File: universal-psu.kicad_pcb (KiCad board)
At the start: 2 copper layers, 64 parts, among them J1 Screw_Terminal_01x04, J2 Screw_Terminal_01x04, J3 Screw_Terminal_01x04

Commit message: layout changes
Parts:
- moved C15 139.9 mm to (264.7, 138.4)
- moved C18 139.9 mm to (258.2, 118.3)
- moved C19 139.9 mm to (258.2, 122.6)
- moved C20 139.9 mm to (258.2, 126.8)
- moved C22 139.9 mm to (264.7, 140.2)
- moved PS3 139.9 mm to (263.1, 133.2)
- moved R12 139.9 mm to (247.6, 120.0)
- moved R15 139.9 mm to (247.6, 127.5)
- moved 12V2 139.9 mm to (251.8, 131.0)
- moved 3v3 139.9 mm to (255.8, 139.1)
- moved 3v3_FB1 139.9 mm to (251.8, 139.1)
- moved 3v3_RT1 139.9 mm to (255.8, 131.0)
- moved C13 139.9 mm to (252.6, 118.3)
- moved C14 139.9 mm to (252.6, 122.6)
- moved C16 139.9 mm to (259.7, 140.3)
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- renumbered TP1 to 12V1, TP8 to 12V2, TP14 to 3v3, TP10 to 3v3_FB1, TP12 to 3v3_RT1, TP7 to 5V1, TP3 to 5V_FB1, TP5 to 5V_RT1, TP2 to GND1, TP4 to GND2, TP6 to GND3, TP9 to GND4, TP11 to GND5, TP13 to GND6
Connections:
- R8 pad 1: +5V -> +3V3
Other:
- copper layers 2 -> 4

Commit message: more  layout
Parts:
- moved C16 171.3 mm to (178.1, -10.3)
- moved C18 171.3 mm to (176.6, -32.2)
- moved C19 171.3 mm to (176.6, -28.0)
- moved C20 171.3 mm to (176.6, -23.8)
- moved GND4 171.3 mm to (170.2, -15.6)
- moved GND6 171.3 mm to (174.2, -15.6)
- moved R18 171.3 mm to (165.9, -15.6)
- moved 12V2 171.3 mm to (170.2, -19.6)
- moved 3v3 171.3 mm to (174.2, -11.5)
- moved 3v3_FB1 171.3 mm to (170.2, -11.5)
- moved 3v3_RT1 171.3 mm to (174.2, -19.6)
- moved C13 171.3 mm to (170.9, -32.2)
- moved C14 171.3 mm to (170.9, -28.0)
- moved C15 171.3 mm to (183.1, -12.2)
- moved C17 171.3 mm to (170.9, -23.8)
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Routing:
- net /DC_DC_Converter_5V/FB: track 0.00 -> 19.0 mm
- net /DC_DC_Converter_5V/Vosns: track 0.00 -> 12.7 mm
- net /DC_DC_Converter_5V/Vcc: track 0.00 -> 11.4 mm
- net /DC_DC_Converter_5V/COMP: track 0.00 -> 10.5 mm
- net /DC_DC_Converter_5V/RT: track 0.00 -> 10.0 mm
- net /DC_DC_Converter_5V/PG: track 0.00 -> 9.96 mm
- net Net-(C7-Pad1): track 0.00 -> 9.04 mm
- net /DC_DC_Converter_5V/Enable: track 0.00 -> 7.95 mm, vias 0 -> 2
- net /DC_DC_Converter_5V/CONFIG: track 0.00 -> 7.03 mm
- net Net-(C3-Pad1): track 0.00 -> 4.17 mm

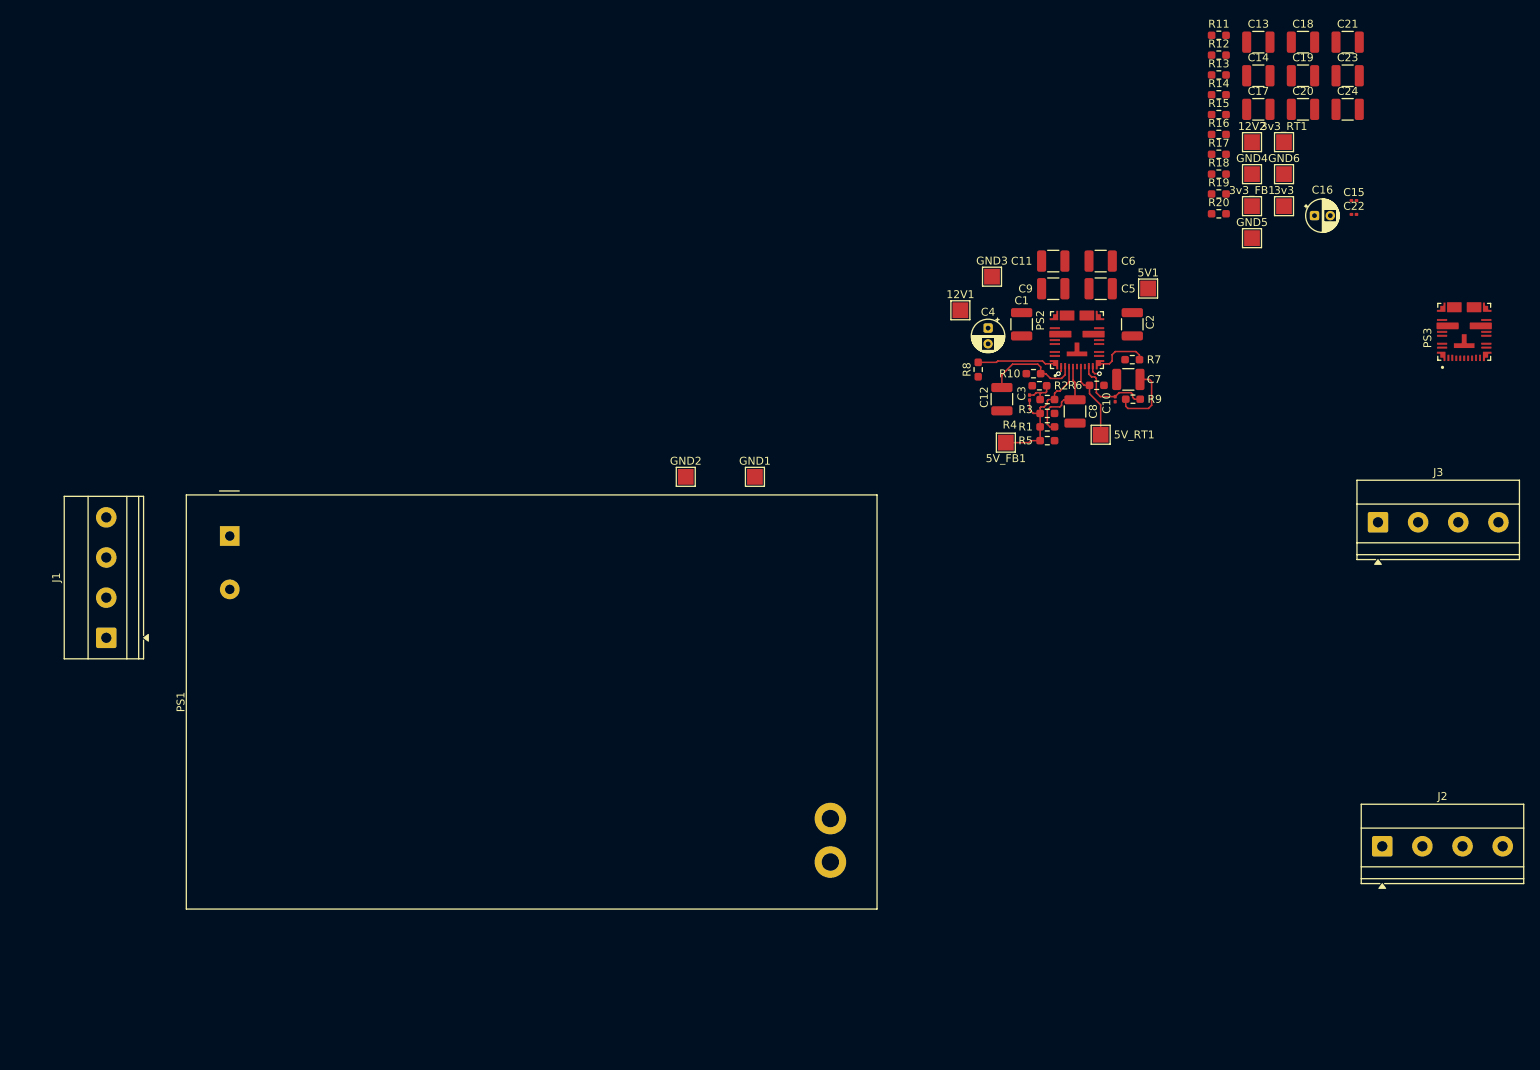
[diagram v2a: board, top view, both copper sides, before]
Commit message: Layout  closed, some DRC  conflicts remain.
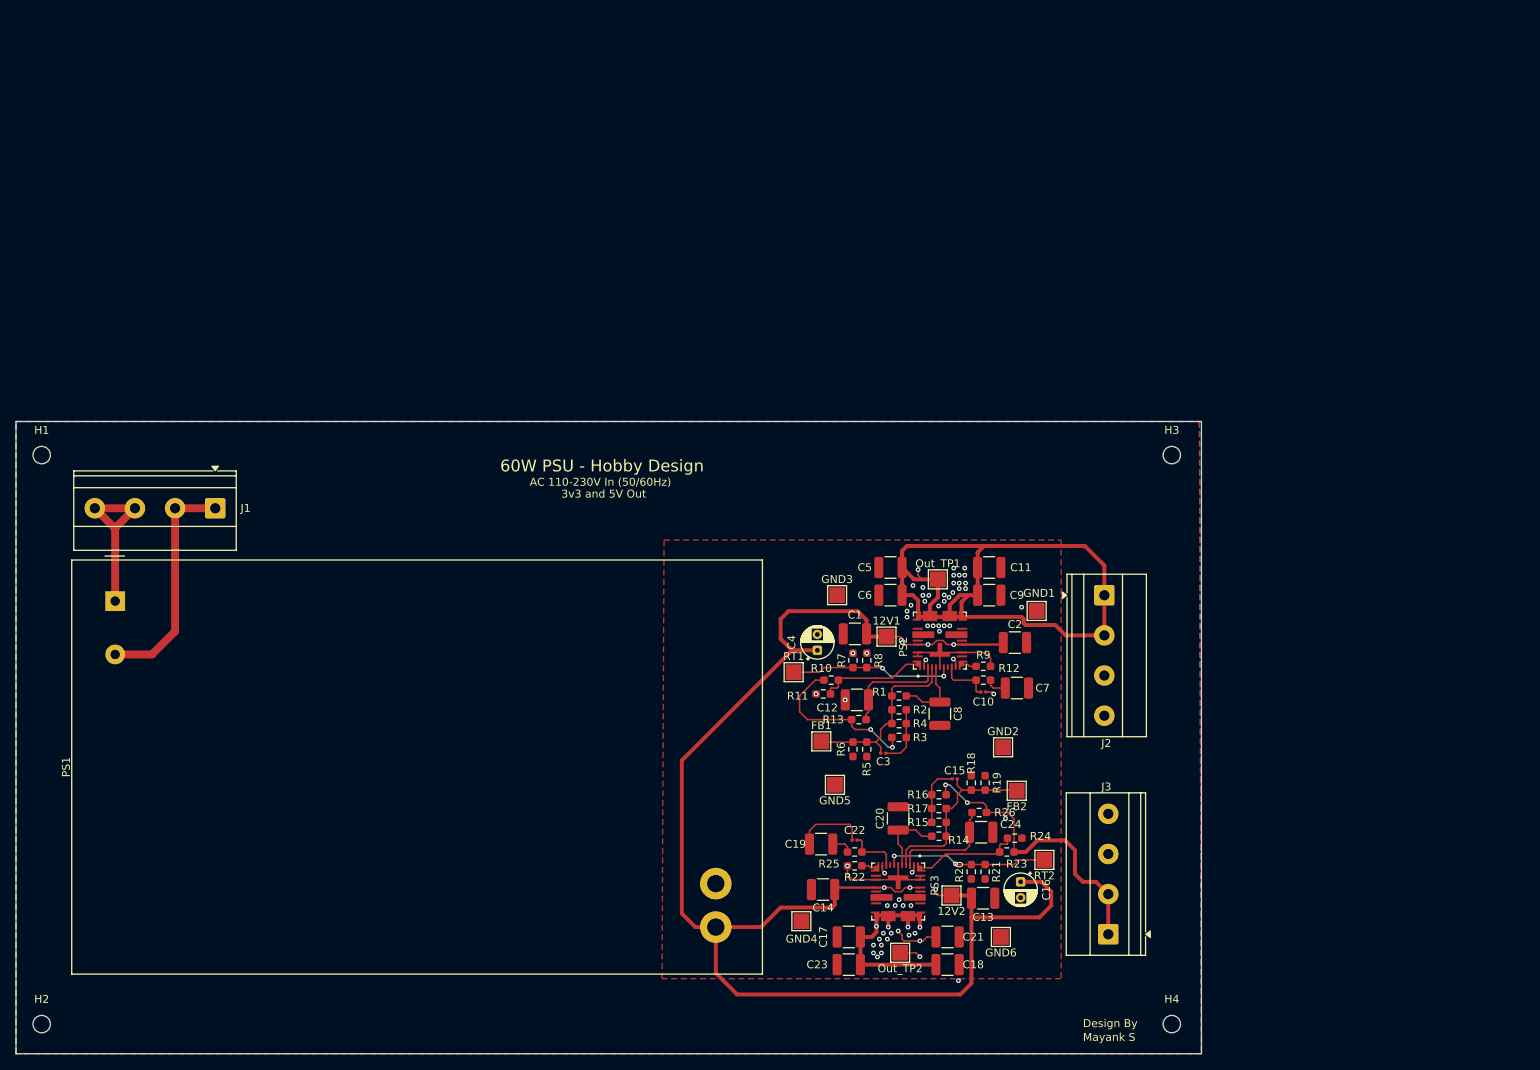
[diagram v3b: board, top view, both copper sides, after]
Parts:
- removed 3v3, 5V1: 5V, TestPoint:TestPoint_Pad_2.0x2.0mm
- removed 3v3_FB1, 5V_FB1: FB, TestPoint:TestPoint_Pad_2.0x2.0mm
- removed 3v3_RT1, 5V_RT1: RT, TestPoint:TestPoint_Pad_2.0x2.0mm
- added FB1: FB, TestPoint:TestPoint_Pad_2.0x2.0mm, F.Cu at (115.7, 56.2)
- added FB2: FB, TestPoint:TestPoint_Pad_2.0x2.0mm, F.Cu at (140.4, 62.5)
- added H1: MH_Pad_MP, MountingHole:MountingHole_2.2mm_M2, F.Cu at (17.0, 20.0)
- added H2: MH_Pad_MP, MountingHole:MountingHole_2.2mm_M2, F.Cu at (17.0, 92.0)
- added H3: MH_Pad_MP, MountingHole:MountingHole_2.2mm_M2, F.Cu at (160.0, 20.0)
- added H4: MH_Pad_MP, MountingHole:MountingHole_2.2mm_M2, F.Cu at (160.0, 92.0)
- added Out_TP1: 5V, TestPoint:TestPoint_Pad_2.0x2.0mm, F.Cu at (130.4, 35.7)
- added Out_TP2: 5V, TestPoint:TestPoint_Pad_2.0x2.0mm, F.Cu at (125.6, 83.0)
- added R21: 7.15k_0.21W_0603, Resistor_SMD:R_0603_1608Metric_Pad0.98x0.95mm_HandSolder, F.Cu at (136.4, 72.7)
- added R22: 9.53k_0.21W_0603, Resistor_SMD:R_0603_1608Metric_Pad0.98x0.95mm_HandSolder, F.Cu at (119.9, 72.0)
- added R23: 10k_0.21W_0603, Resistor_SMD:R_0603_1608Metric_Pad0.98x0.95mm_HandSolder, F.Cu at (139.1, 70.2)
- added R24: 10k_0.21W_0603, Resistor_SMD:R_0603_1608Metric_Pad0.98x0.95mm_HandSolder, F.Cu at (140.1, 68.5)
- added R25: 11k_0.21W_0603, Resistor_SMD:R_0603_1608Metric_Pad0.98x0.95mm_HandSolder, F.Cu at (119.9, 70.2)
- added R26: 0_0.21W_0603, Resistor_SMD:R_0603_1608Metric_Pad0.98x0.95mm_HandSolder, F.Cu at (135.6, 65.2)
- added RT1: RT, TestPoint:TestPoint_Pad_2.0x2.0mm, F.Cu at (112.2, 47.5)
- added RT2: RT, TestPoint:TestPoint_Pad_2.0x2.0mm, F.Cu at (143.9, 71.2)
- R10, R5: value 0_0.21W_0603 -> 10k_0.21W_0603
- R12: value 100_0.21W_0603 -> 11k_0.21W_0603
- R13: value 31.6k_0.21W_0603 -> 0_0.21W_0603
- R15, R20: value 0_0.21W_0603 -> 31.6k_0.21W_0603
- R16: value 31.6k_0.21W_0603 -> 100_0.21W_0603
- R17: value 9.53k_0.21W_0603 -> 52.3k_0.21W_0603
- R19: value 11k_0.21W_0603 -> 0_0.21W_0603
- R2: value 100_0.21W_0603 -> 31.6k_0.21W_0603
- R3: value 52.3k_0.21W_0603 -> 100_0.21W_0603
- R4: value 10k_0.21W_0603 -> 52.3k_0.21W_0603
- R6: value 7.15k_0.21W_0603 -> 0_0.21W_0603
- R7: value 9.53k_0.21W_0603 -> 31.6k_0.21W_0603
- R8: value 10k_0.21W_0603 -> 7.15k_0.21W_0603
- R9: value 11k_0.21W_0603 -> 9.53k_0.21W_0603
- moved C23 129.0 mm to (119.1, 84.5), turned to 180 degrees
- moved C18 125.1 mm to (131.6, 84.5)
- moved C21 124.0 mm to (131.6, 81.0)
- moved C17 116.8 mm to (119.1, 81.0), turned to 180 degrees
- moved C14 116.8 mm to (115.9, 75.0), turned to 180 degrees
- moved C19 114.8 mm to (115.6, 69.2), turned to 180 degrees
- moved C13 113.8 mm to (136.1, 76.1)
- moved GND4 110.4 mm to (113.1, 79.0), turned to 180 degrees
- moved C20 103.3 mm to (125.4, 66.0), turned to 90 degrees
- moved GND6 103.0 mm to (138.4, 81.0), turned to 180 degrees
- moved 12V2 102.6 mm to (132.1, 75.7), turned to 180 degrees
- moved C24 102.6 mm to (135.9, 67.7)
- moved C22 101.3 mm to (119.9, 68.7), turned to 180 degrees
- moved PS3 100.7 mm to (125.4, 75.2), turned to -90 degrees
- moved R14 100.3 mm to (130.5, 68.2)
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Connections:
- C10 pad 1: /DC_DC_Converter_5V/COMP -> /DC_DC_Converter_3v3/COMP
- C11 pad 1: +5V -> +3V3
- C12 pad 1: /DC_DC_Converter_5V/Vosns -> /DC_DC_Converter_3v3/Vosns
- C15 pad 2: /DC_DC_Converter_3v3/FB -> /DC_DC_Converter_5V/FB
- C17 pad 1: +3V3 -> +5V
- C18 pad 1: +3V3 -> +5V
- C20 pad 1: /DC_DC_Converter_3v3/Vcc -> /DC_DC_Converter_5V/Vcc
- C21 pad 1: +3V3 -> +5V
- C22 pad 1: /DC_DC_Converter_3v3/COMP -> /DC_DC_Converter_5V/COMP
- C23 pad 1: +3V3 -> +5V
- C24 pad 1: /DC_DC_Converter_3v3/Vosns -> /DC_DC_Converter_5V/Vosns
- C3 pad 2: /DC_DC_Converter_5V/FB -> /DC_DC_Converter_3v3/FB
- C5 pad 1: +5V -> +3V3
- C6 pad 1: +5V -> +3V3
- C8 pad 1: /DC_DC_Converter_5V/Vcc -> /DC_DC_Converter_3v3/Vcc
- C9 pad 1: +5V -> +3V3
- PS2 pad 1: /DC_DC_Converter_5V/PG -> /DC_DC_Converter_3v3/PG
- PS2 pad 10: /DC_DC_Converter_5V/Enable -> /DC_DC_Converter_3v3/Enable
- PS2 pad 11: /DC_DC_Converter_5V/CONFIG -> /DC_DC_Converter_3v3/CONFIG
- PS2 pad 18: +5V -> +3V3
- PS2 pad 19: +5V -> +3V3
- PS2 pad 2: /DC_DC_Converter_5V/Enable -> /DC_DC_Converter_3v3/Enable
- PS2 pad 20: +5V -> +3V3
- PS2 pad 21: +5V -> +3V3
- PS2 pad 3: /DC_DC_Converter_5V/Vosns -> /DC_DC_Converter_3v3/Vosns
- PS2 pad 4: /DC_DC_Converter_5V/FB -> /DC_DC_Converter_3v3/FB
- PS2 pad 5: /DC_DC_Converter_5V/Vcc -> /DC_DC_Converter_3v3/Vcc
- PS2 pad 7: /DC_DC_Converter_5V/RT -> /DC_DC_Converter_3v3/RT
- PS2 pad 9: /DC_DC_Converter_5V/COMP -> /DC_DC_Converter_3v3/COMP
- PS3 pad 1: /DC_DC_Converter_3v3/PG -> /DC_DC_Converter_5V/PG
- PS3 pad 10: /DC_DC_Converter_3v3/Enable -> /DC_DC_Converter_5V/Enable
- PS3 pad 11: /DC_DC_Converter_3v3/CONFIG -> /DC_DC_Converter_5V/CONFIG
- PS3 pad 18: +3V3 -> +5V
- PS3 pad 19: +3V3 -> +5V
- PS3 pad 2: /DC_DC_Converter_3v3/Enable -> /DC_DC_Converter_5V/Enable
- PS3 pad 20: +3V3 -> +5V
- PS3 pad 21: +3V3 -> +5V
- PS3 pad 3: /DC_DC_Converter_3v3/Vosns -> /DC_DC_Converter_5V/Vosns
- PS3 pad 4: /DC_DC_Converter_3v3/FB -> /DC_DC_Converter_5V/FB
- PS3 pad 5: /DC_DC_Converter_3v3/Vcc -> /DC_DC_Converter_5V/Vcc
- PS3 pad 7: /DC_DC_Converter_3v3/RT -> /DC_DC_Converter_5V/RT
- PS3 pad 9: /DC_DC_Converter_3v3/COMP -> /DC_DC_Converter_5V/COMP
- R1 pad 1: /DC_DC_Converter_5V/Vcc -> /DC_DC_Converter_3v3/Vcc
- R1 pad 2: /DC_DC_Converter_5V/FB -> /DC_DC_Converter_3v3/FB
- R10 pad 1: +5V -> +3V3
- R10 pad 2: /DC_DC_Converter_5V/Vosns -> /DC_DC_Converter_3v3/PG
- R11 pad 1: /DC_DC_Converter_3v3/Vcc -> /DC_DC_Converter_3v3/PG
- R11 pad 2: /DC_DC_Converter_3v3/FB -> GND
- R12 pad 1: +3V3 -> /DC_DC_Converter_3v3/COMP
- R12 pad 2: Net-(C15-Pad1) -> Net-(C7-Pad1)
- R13 pad 1: Net-(C15-Pad1) -> +3V3
- R13 pad 2: /DC_DC_Converter_3v3/FB -> /DC_DC_Converter_3v3/Vosns
- R14 pad 1: /DC_DC_Converter_3v3/FB -> /DC_DC_Converter_5V/Vcc
- R14 pad 2: GND -> /DC_DC_Converter_5V/FB
- R15 pad 1: /DC_DC_Converter_3v3/FB -> Net-(C15-Pad1)
- R15 pad 2: GND -> /DC_DC_Converter_5V/FB
- R16 pad 1: /DC_DC_Converter_3v3/RT -> +5V
- R16 pad 2: GND -> Net-(C15-Pad1)
- R17 pad 1: /DC_DC_Converter_3v3/CONFIG -> Net-(C15-Pad1)
- R17 pad 2: GND -> /DC_DC_Converter_5V/FB
- R18 pad 1: +3V3 -> /DC_DC_Converter_5V/FB
- R18 pad 2: /DC_DC_Converter_3v3/PG -> GND
- R19 pad 1: /DC_DC_Converter_3v3/COMP -> /DC_DC_Converter_5V/FB
- R19 pad 2: Net-(C19-Pad1) -> GND
- R2 pad 1: +5V -> Net-(C3-Pad1)
- R2 pad 2: Net-(C3-Pad1) -> /DC_DC_Converter_3v3/FB
- R20 pad 1: +3V3 -> /DC_DC_Converter_5V/RT
- R20 pad 2: /DC_DC_Converter_3v3/Vosns -> GND
- R3 pad 1: Net-(C3-Pad1) -> +3V3
- R3 pad 2: /DC_DC_Converter_5V/FB -> Net-(C3-Pad1)
- R4 pad 1: /DC_DC_Converter_5V/FB -> Net-(C3-Pad1)
- R4 pad 2: GND -> /DC_DC_Converter_3v3/FB
- R5 pad 1: /DC_DC_Converter_5V/FB -> /DC_DC_Converter_3v3/FB
- R6 pad 1: /DC_DC_Converter_5V/RT -> /DC_DC_Converter_3v3/FB
- R7 pad 1: /DC_DC_Converter_5V/CONFIG -> /DC_DC_Converter_3v3/RT
- R8 pad 1: +3V3 -> /DC_DC_Converter_3v3/RT
- R8 pad 2: /DC_DC_Converter_5V/PG -> GND
- R9 pad 1: /DC_DC_Converter_5V/COMP -> /DC_DC_Converter_3v3/CONFIG
- R9 pad 2: Net-(C7-Pad1) -> GND
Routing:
- net +12V: track 0.00 -> 186.4 mm, vias 0 -> 6
- net +3V3: track 0.00 -> 146.4 mm, vias 0 -> 3
- net +5V: track 0.00 -> 128.4 mm, vias 0 -> 9
- net GND: track 0.00 -> 36.1 mm, vias 0 -> 54
- net AC_In_Neutral: track 0.00 -> 29.5 mm
- net /DC_DC_Converter_3v3/FB: track 0.00 -> 23.9 mm
- net AC_In_Live: track 0.00 -> 21.5 mm
- net /DC_DC_Converter_3v3/RT: track 0.00 -> 20.8 mm, vias 0 -> 2
- net /DC_DC_Converter_3v3/Vosns: track 0.00 -> 13.9 mm
- net /DC_DC_Converter_3v3/PG: track 0.00 -> 13.5 mm
- net /DC_DC_Converter_5V/RT: track 10.0 -> 20.8 mm, vias 0 -> 2
- net /DC_DC_Converter_3v3/Vcc: track 0.00 -> 9.20 mm
- net Net-(C15-Pad1): track 0.00 -> 7.65 mm
- net /DC_DC_Converter_3v3/COMP: track 0.00 -> 6.64 mm
- net Net-(C7-Pad1): track 9.04 -> 2.66 mm
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- added copper zone on F.Cu, net +12V
- added copper zone on In1.Cu, net +3V3
- added copper zone on In2.Cu, net +5V
- added copper zone on B.Cu, net GND
- added copper zone on F.Cu, net GND
- added copper zone on In1.Cu, net GND
- added copper zone on In2.Cu, net GND
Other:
- board outline added: 150 x 80 mm
- board text added: "3v3 and 5V Out"
- board text added: "60W PSU - Hobby Design"
- board text added: "AC 110-230V In (50/60Hz)"
- board text added: "Design By"
- board text added: "Mayank S"
- board text added: "Thermal vias pending for TLVM14406"

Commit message: hopefully final  design output, time  for manufacturing
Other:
- board text removed: "Thermal vias pending for TLVM14406"

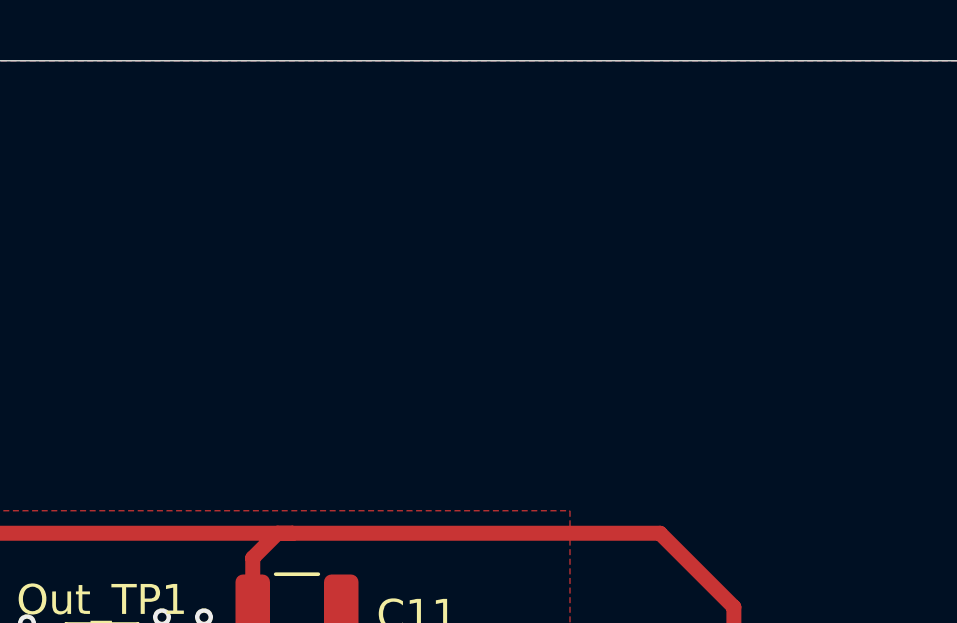
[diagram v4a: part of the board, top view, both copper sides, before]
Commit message: docs: Add comprehensive README with specs, safety warnings, and project structure with license on the silkscreen cos why not
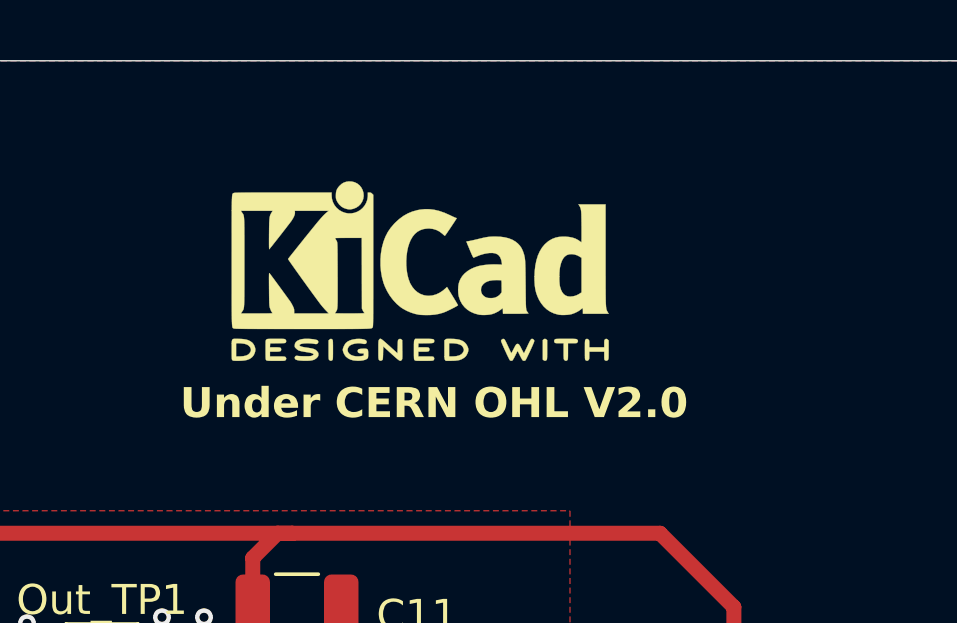
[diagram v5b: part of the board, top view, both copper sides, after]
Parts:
- added REF**: KiCad-Logo2_5mm_SilkScreen, Symbol:KiCad-Logo2_5mm_SilkScreen, F.Cu at (141.0, 22.8)
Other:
- board text added: "Under CERN OHL V2.0"

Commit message: updated images
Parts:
- added REF**: OSHW-Logo2_7.3x6mm_SilkScreen, Symbol:OSHW-Logo2_7.3x6mm_SilkScreen, F.Cu at (126.8, 23.2)
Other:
- board text removed: "Under CERN OHL V2.0"
